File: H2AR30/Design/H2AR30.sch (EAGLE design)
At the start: 57 parts, among them P1 HEXABIT__NO_P1_P5_P6_P7_P12, U2 INA199B2DCKT, U3 INA199B1DCKT, U4 TEXAS_INSTRUMENTS_REF2033AIDD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, X1 XTALL_CSTCE8M00G52

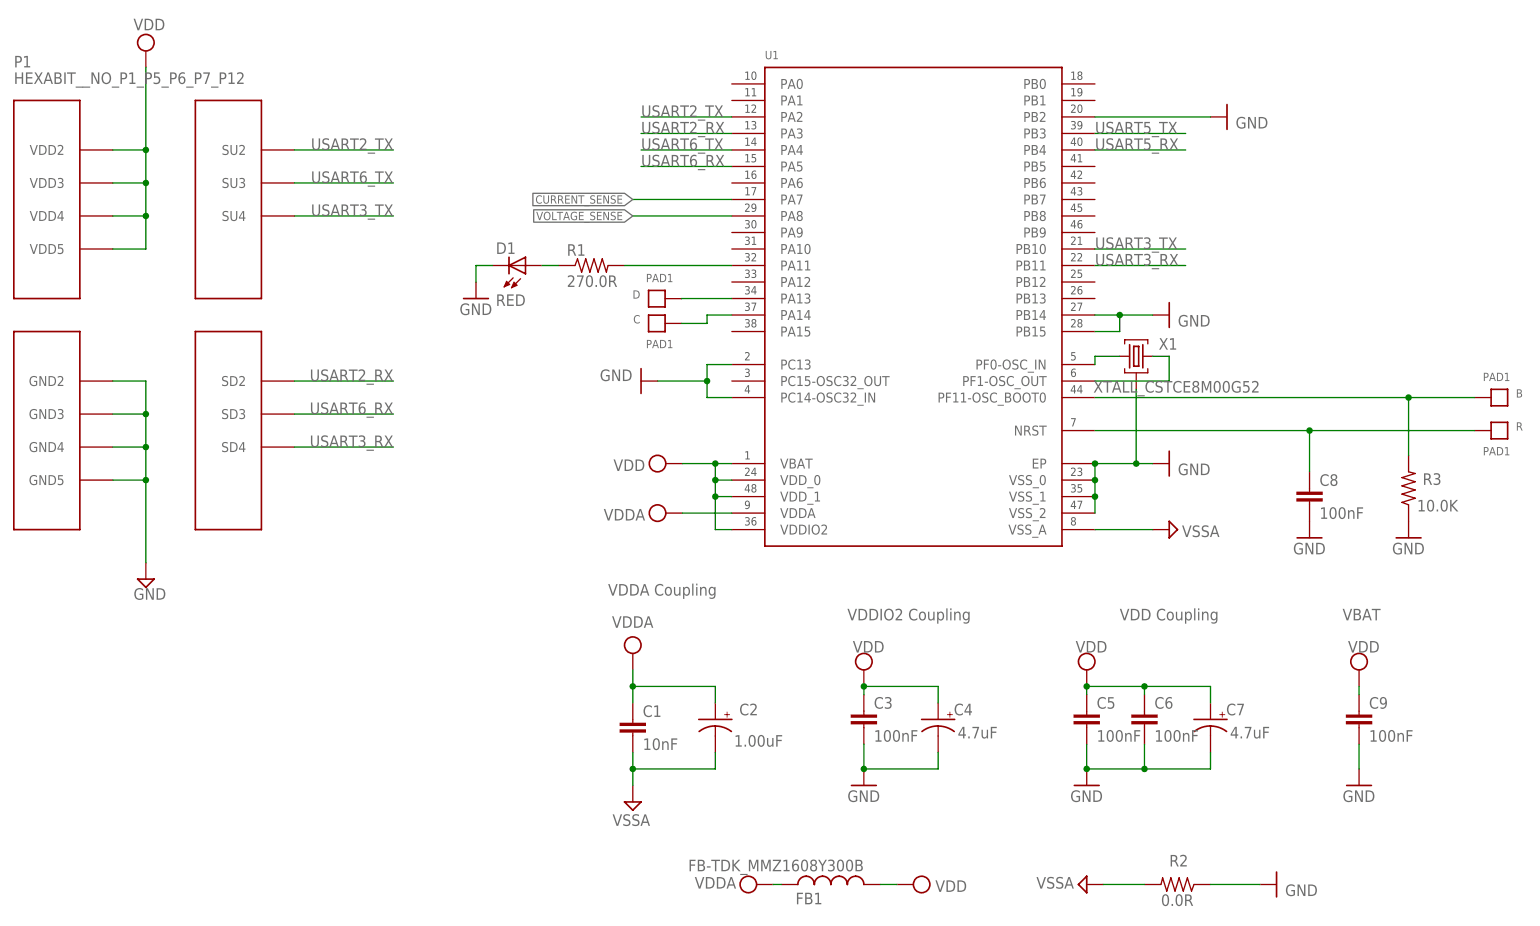
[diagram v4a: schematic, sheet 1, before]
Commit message: Final Design: High voltage logos were added High voltage clearance checked * were added to boot pins 100A & 4A (optional ) CTs  were added to BOM ERC & DRC were made
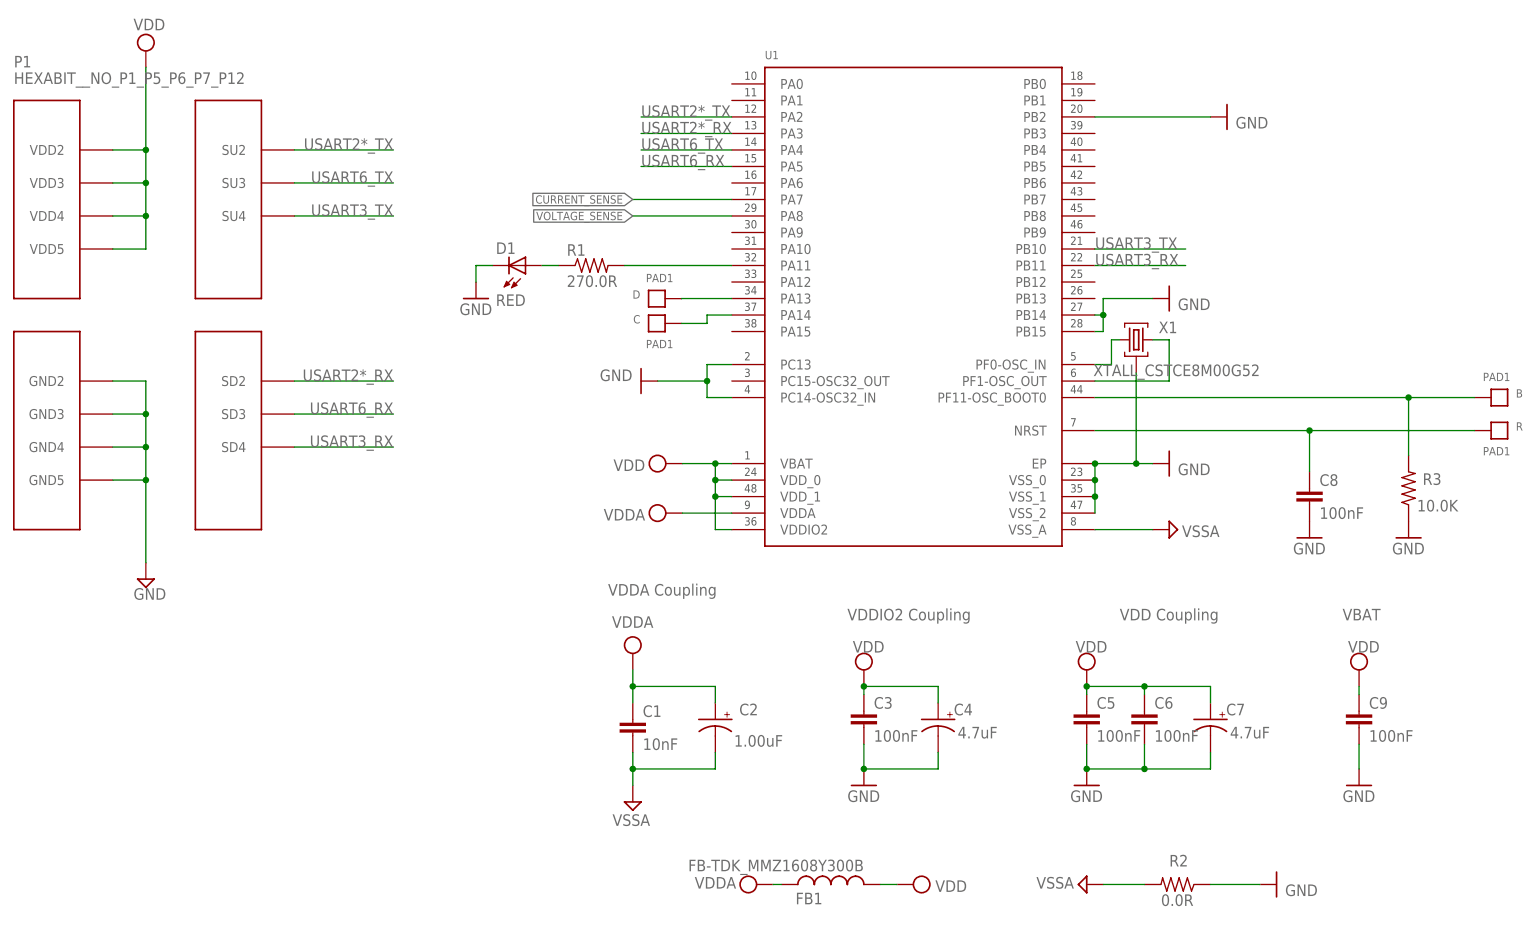
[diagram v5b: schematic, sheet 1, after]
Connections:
- net USART2_RX renamed USART2*_RX
- net USART2_TX renamed USART2*_TX
- removed net USART5_RX: U1.PB4
- removed net USART5_TX: U1.PB3
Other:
- moved on the sheet: X1
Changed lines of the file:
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@@
 <setting verticaltext="up"/>
 </settings>
-<grid distance="0.1" unitdist="inch" unit="inch" style="lines" multiple="1" display="no" altdistance="0.01" altunitdist="inch" altunit="inch"/>
+<grid distance="50" unitdist="mil" unit="mil" style="lines" multiple="1" display="no" altdistance="0.01" altunitdist="inch" altunit="inch"/>
 <layers>
 <layer number="1" name="Top" color="4" fill="1" visible="no" active="no"/>
@@
 <attribute name="OCTOPART_URL" value="https://octopart.com/rt1206brd071ml-yageo-1262221?r=sp"/>
 </part>
-<part name="U3" library="HEXABITZ_ICs" library_urn="urn:adsk.eagle:library:20064554" deviceset="INA199B1DCKT" device="" package3d_urn="urn:adsk.eagle:package:19904117/2" value="INA199B1DCKT"/>
+<part name="U3" library="HEXABITZ_ICs" library_urn="urn:adsk.eagle:library:20064554" deviceset="INA199B1DCKT" device="" package3d_urn="urn:adsk.eagle:package:19904117/4" value="INA199B1DCKT"/>
 <part name="C16" library="HEXABITZ_RCLS" library_urn="urn:adsk.eagle:library:20064561" deviceset="C-0603" device="" package3d_urn="urn:adsk.eagle:package:19666468/2" value="10uF">
 <attribute name="CAPACITANCE" value="10uF"/>
@@
 <part name="GND11" library="supply1" library_urn="urn:adsk.eagle:library:371" deviceset="GND" device=""/>
 <part name="P1" library="hexabitz_connectors" library_urn="urn:adsk.eagle:library:20064578" deviceset="HEXABIT_?_NO_P1_P5_P6_P7_P12" device="" package3d_urn="urn:adsk.eagle:package:20748456/3"/>
-<part name="U2" library="HEXABITZ_ICs" library_urn="urn:adsk.eagle:library:20064554" deviceset="INA199B2DCKT" device="" package3d_urn="urn:adsk.eagle:package:19904117/2"/>
+<part name="U2" library="HEXABITZ_ICs" library_urn="urn:adsk.eagle:library:20064554" deviceset="INA199B2DCKT" device="" package3d_urn="urn:adsk.eagle:package:19904117/4"/>
 </parts>
 <sheets>
@@
 <attribute name="VALUE" x="99.568" y="145.415" size="1.778" layer="96" rot="MR180"/>
 </instance>
-<instance part="X1" gate="G$1" x="198.12" y="135.89" smashed="yes">
-<attribute name="NAME" x="204.47" y="138.684" size="1.778" layer="95" rot="R180"/>
-<attribute name="VALUE" x="217.17" y="132.08" size="1.778" layer="96" rot="R180"/>
+<instance part="X1" gate="G$1" x="198.12" y="138.43" smashed="yes">
+<attribute name="NAME" x="204.47" y="141.224" size="1.778" layer="95" rot="R180"/>
+<attribute name="VALUE" x="217.17" y="134.62" size="1.778" layer="96" rot="R180"/>
 </instance>
 <instance part="GND1" gate="1" x="96.52" y="144.78" smashed="yes">
@@
 <attribute name="VALUE" x="43.815" y="98.425" size="1.778" layer="96"/>
 </instance>
-<instance part="GND9" gate="1" x="203.2" y="142.24" smashed="yes" rot="R90">
-<attribute name="VALUE" x="209.55" y="142.24" size="1.778" layer="96" rot="R180"/>
+<instance part="GND9" gate="1" x="203.2" y="144.78" smashed="yes" rot="R90">
+<attribute name="VALUE" x="209.55" y="144.78" size="1.778" layer="96" rot="R180"/>
 </instance>
 <instance part="GND10" gate="1" x="121.92" y="132.08" smashed="yes" rot="R270">
@@
 <wire x1="191.77" y1="114.3" x2="191.77" y2="116.84" width="0.1524" layer="91"/>
 <wire x1="191.77" y1="116.84" x2="191.77" y2="119.38" width="0.1524" layer="91"/>
-<wire x1="198.12" y1="130.81" x2="198.12" y2="119.38" width="0.1524" layer="91"/>
+<wire x1="198.12" y1="133.35" x2="198.12" y2="119.38" width="0.1524" layer="91"/>
 <junction x="191.77" y="119.38"/>
 <pinref part="U1" gate="G$1" pin="VSS_0"/>
@@
 </segment>
 <segment>
-<pinref part="GND9" gate="1" pin="GND"/>
-<wire x1="200.66" y1="142.24" x2="195.58" y2="142.24" width="0.1524" layer="91"/>
-<pinref part="U1" gate="G$1" pin="PB14"/>
-<pinref part="U1" gate="G$1" pin="PB15"/>
-<wire x1="195.58" y1="142.24" x2="191.77" y2="142.24" width="0.1524" layer="91"/>
-<wire x1="191.77" y1="139.7" x2="195.58" y2="139.7" width="0.1524" layer="91"/>
-<wire x1="195.58" y1="139.7" x2="195.58" y2="142.24" width="0.1524" layer="91"/>
-<junction x="195.58" y="142.24"/>
-</segment>
-<segment>
 <pinref part="U1" gate="G$1" pin="PC14-OSC32_IN"/>
 <wire x1="135.89" y1="129.54" x2="132.08" y2="129.54" width="0.1524" layer="91"/>
@@
 <wire x1="191.77" y1="172.72" x2="209.55" y2="172.72" width="0.1524" layer="91"/>
 </segment>
-</net>
-<net name="USART5_TX" class="0">
-<segment>
-<pinref part="U1" gate="G$1" pin="PB3"/>
-<wire x1="191.77" y1="170.18" x2="205.74" y2="170.18" width="0.1524" layer="91"/>
-<label x="191.77" y="170.18" size="1.778" layer="95"/>
-</segment>
-</net>
-<net name="USART5_RX" class="0">
 <segment>
-<pinref part="U1" gate="G$1" pin="PB4"/>
-<wire x1="191.77" y1="167.64" x2="205.74" y2="167.64" width="0.1524" layer="91"/>
-<label x="191.77" y="167.64" size="1.778" layer="95"/>
+<pinref part="U1" gate="G$1" pin="PB14"/>
+<pinref part="U1" gate="G$1" pin="PB15"/>
+<wire x1="193.04" y1="142.24" x2="191.77" y2="142.24" width="0.1524" layer="91"/>
+<wire x1="191.77" y1="139.7" x2="193.04" y2="139.7" width="0.1524" layer="91"/>
+<wire x1="193.04" y1="139.7" x2="193.04" y2="142.24" width="0.1524" layer="91"/>
+<wire x1="193.04" y1="142.24" x2="193.04" y2="144.78" width="0.1524" layer="91"/>
+<junction x="193.04" y="142.24"/>
+<pinref part="GND9" gate="1" pin="GND"/>
+<wire x1="193.04" y1="144.78" x2="200.66" y2="144.78" width="0.1524" layer="91"/>
 </segment>
 </net>
@@
 <net name="N$5" class="0">
 <segment>
-<pinref part="U1" gate="G$1" pin="PF0-OSC_IN"/>
-<wire x1="191.77" y1="134.62" x2="191.77" y2="135.89" width="0.1524" layer="91"/>
 <pinref part="X1" gate="G$1" pin="1"/>
-<wire x1="191.77" y1="135.89" x2="195.58" y2="135.89" width="0.1524" layer="91"/>
+<wire x1="194.31" y1="138.43" x2="195.58" y2="138.43" width="0.1524" layer="91"/>
+<pinref part="U1" gate="G$1" pin="PF0-OSC_IN"/>
+<wire x1="191.77" y1="134.62" x2="194.31" y2="134.62" width="0.1524" layer="91"/>
+<wire x1="194.31" y1="134.62" x2="194.31" y2="138.43" width="0.1524" layer="91"/>
 </segment>
 </net>
@@
 <pinref part="U1" gate="G$1" pin="PF1-OSC_OUT"/>
 <wire x1="191.77" y1="132.08" x2="203.2" y2="132.08" width="0.1524" layer="91"/>
-<wire x1="203.2" y1="132.08" x2="203.2" y2="135.89" width="0.1524" layer="91"/>
+<wire x1="203.2" y1="132.08" x2="203.2" y2="138.43" width="0.1524" layer="91"/>
 <pinref part="X1" gate="G$1" pin="3"/>
-<wire x1="203.2" y1="135.89" x2="200.66" y2="135.89" width="0.1524" layer="91"/>
+<wire x1="203.2" y1="138.43" x2="200.66" y2="138.43" width="0.1524" layer="91"/>
 </segment>
 </net>
@@
 </segment>
 </net>
-<net name="USART2_TX" class="0">
+<net name="USART2*_TX" class="0">
 <segment>
 <pinref part="U1" gate="G$1" pin="PA2"/>
@@
 </segment>
 </net>
-<net name="USART2_RX" class="0">
+<net name="USART2*_RX" class="0">
 <segment>
 <pinref part="U1" gate="G$1" pin="PA3"/>
@@
 <wire x1="40.64" y1="181.61" x2="30.48" y2="181.61" width="0.1524" layer="91"/>
 <wire x1="40.64" y1="177.8" x2="40.64" y2="181.61" width="0.1524" layer="91"/>
+<junction x="40.64" y="181.61"/>
 </segment>
 <segment>

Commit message: final with double check
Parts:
- added R16: 1M0, HEXABITZ_RCLS:R_1206R1206
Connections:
- removed net N$24: R10.2, R9.1
- removed net N$25: R8.1, R9.2
- new net N$10: R16.1, R9.2
- new net N$13: R10.2, R8.1
- new net N$22: D3.1, FB5.1, R14.1, R9.1
- net GND: now also U1.PB0
- net NEUTRAL: now also R16.2; no longer D3.1, FB5.1, R14.1
- net VCC: no longer U4.VREF
- net VOLTAGE_SENSE: now also U1.PB1; no longer U1.PA8
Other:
- moved on the sheet: R8, R9
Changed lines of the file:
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@@
 <?xml version="1.0" encoding="utf-8"?>
 <!DOCTYPE eagle SYSTEM "eagle.dtd">
-<eagle version="9.6.1">
+<eagle version="9.6.2">
 <drawing>
 <settings>
@@
 <setting verticaltext="up"/>
 </settings>
-<grid distance="50" unitdist="mil" unit="mil" style="lines" multiple="1" display="no" altdistance="0.01" altunitdist="inch" altunit="inch"/>
+<grid distance="0.05" unitdist="inch" unit="inch" style="lines" multiple="1" display="no" altdistance="0.01" altunitdist="inch" altunit="inch"/>
 <layers>
 <layer number="1" name="Top" color="4" fill="1" visible="no" active="no"/>
@@
 <part name="SUPPLY26" library="supply2" deviceset="VCC" device="" value="VDDA"/>
 <part name="SUPPLY28" library="supply2" deviceset="VCC" device="" value="VDDA"/>
-<part name="SUPPLY32" library="supply2" deviceset="VCC" device="" value="VDDA"/>
 <part name="SUPPLY15" library="supply2" deviceset="AGND" device="" value="VSSA"/>
 <part name="SUPPLY25" library="supply2" deviceset="AGND" device="" value="VSSA"/>
@@
 <part name="P1" library="hexabitz_connectors" library_urn="urn:adsk.eagle:library:20064578" deviceset="HEXABIT_?_NO_P1_P5_P6_P7_P12" device="" package3d_urn="urn:adsk.eagle:package:20748456/3"/>
 <part name="U2" library="HEXABITZ_ICs" library_urn="urn:adsk.eagle:library:20064554" deviceset="INA199B2DCKT" device="" package3d_urn="urn:adsk.eagle:package:19904117/4"/>
+<part name="R16" library="HEXABITZ_RCLS" library_urn="urn:adsk.eagle:library:20064561" deviceset="R_1206" device="R1206" package3d_urn="urn:adsk.eagle:package:20937486/1" value="1M0">
+<spice>
+<pinmapping spiceprefix="R">
+<pinmap gate="G$1" pin="1" pinorder="1"/>
+<pinmap gate="G$1" pin="2" pinorder="2"/>
+</pinmapping>
+</spice>
+<attribute name="MFN" value="Yageo"/>
+<attribute name="MPN" value="RT1206BRD071ML"/>
+<attribute name="OCTOPART_URL" value="https://octopart.com/rt1206brd071ml-yageo-1262221?r=sp"/>
+</part>
+<part name="GND12" library="supply1" library_urn="urn:adsk.eagle:library:371" deviceset="GND" device=""/>
 </parts>
 <sheets>
@@
 <attribute name="VALUE" x="25.4" y="177.8" size="1.778" layer="96"/>
 </instance>
+<instance part="GND12" gate="1" x="212.09" y="177.8" smashed="yes" rot="R90">
+<attribute name="VALUE" x="218.44" y="177.8" size="1.778" layer="96" rot="R180"/>
+</instance>
 </instances>
 <busses>
@@
 <wire x1="193.04" y1="144.78" x2="200.66" y2="144.78" width="0.1524" layer="91"/>
 </segment>
+<segment>
+<pinref part="U1" gate="G$1" pin="PB0"/>
+<pinref part="GND12" gate="1" pin="GND"/>
+<wire x1="191.77" y1="177.8" x2="209.55" y2="177.8" width="0.1524" layer="91"/>
+</segment>
 </net>
 <net name="USART3_TX" class="0">
@@
 <net name="VOLTAGE_SENSE" class="0">
 <segment>
-<pinref part="U1" gate="G$1" pin="PA8"/>
-<wire x1="135.89" y1="157.48" x2="120.65" y2="157.48" width="0.1524" layer="91"/>
-<label x="120.65" y="157.48" size="1.27" layer="95" rot="R180" xref="yes"/>
+<pinref part="U1" gate="G$1" pin="PB1"/>
+<wire x1="191.77" y1="175.26" x2="223.52" y2="175.26" width="0.1524" layer="91"/>
+<label x="223.52" y="175.26" size="1.27" layer="95" xref="yes"/>
 </segment>
 </net>
@@
 <attribute name="VALUE" x="110.617" y="159.385" size="1.778" layer="96" rot="R180"/>
 </instance>
-<instance part="R8" gate="G$1" x="41.91" y="129.54" smashed="yes" rot="R90">
-<attribute name="NAME" x="44.45" y="132.3086" size="1.778" layer="95"/>
-<attribute name="VALUE" x="44.45" y="126.238" size="1.778" layer="96"/>
-</instance>
-<instance part="R9" gate="G$1" x="41.91" y="116.84" smashed="yes" rot="R90">
+<instance part="R8" gate="G$1" x="41.91" y="116.84" smashed="yes" rot="R90">
 <attribute name="NAME" x="44.45" y="119.6086" size="1.778" layer="95"/>
 <attribute name="VALUE" x="44.45" y="113.538" size="1.778" layer="96"/>
 </instance>
+<instance part="R9" gate="G$1" x="34.29" y="86.36" smashed="yes" rot="R180">
+<attribute name="NAME" x="31.5214" y="88.9" size="1.778" layer="95" rot="R90"/>
+<attribute name="VALUE" x="37.592" y="88.9" size="1.778" layer="96" rot="R90"/>
+</instance>
 <instance part="R10" gate="G$1" x="41.91" y="104.14" smashed="yes" rot="R90">
 <attribute name="NAME" x="44.45" y="106.9086" size="1.778" layer="95"/>
@@
 <attribute name="VALUE" x="173.355" y="73.025" size="1.778" layer="96" rot="R180"/>
 </instance>
-<instance part="SUPPLY32" gate="G$1" x="208.28" y="52.07" smashed="yes" rot="R270">
-<attribute name="VALUE" x="213.995" y="48.895" size="1.778" layer="96" rot="R90"/>
-</instance>
 <instance part="SUPPLY15" gate="G$1" x="125.73" y="34.29" smashed="yes">
 <attribute name="VALUE" x="128.397" y="32.385" size="1.778" layer="96" rot="R180"/>
@@
 <attribute name="VALUE" x="171.2976" y="143.0782" size="2.0828" layer="96" ratio="10" rot="SR0"/>
 </instance>
+<instance part="R16" gate="G$1" x="22.86" y="86.36" smashed="yes" rot="R180">
+<attribute name="NAME" x="20.0914" y="88.9" size="1.778" layer="95" rot="R90"/>
+<attribute name="VALUE" x="26.162" y="88.9" size="1.778" layer="96" rot="R90"/>
+</instance>
 </instances>
 <busses>
@@
 </segment>
 <segment>
-<pinref part="U4" gate="G$0" pin="VREF"/>
-<wire x1="205.74" y1="52.07" x2="205.74" y2="52.324" width="0.1524" layer="91"/>
-<wire x1="205.74" y1="52.324" x2="204.47" y2="52.324" width="0.1524" layer="91"/>
-<pinref part="SUPPLY32" gate="G$1" pin="VCC"/>
-</segment>
-<segment>
 <pinref part="SUPPLY14" gate="G$1" pin="VCC"/>
 <pinref part="C14" gate="G$1" pin="1"/>
@@
 </segment>
 </net>
-<net name="NEUTRAL" class="0">
+<net name="N$22" class="0">
 <segment>
 <pinref part="D3" gate="G$0" pin="1"/>
@@
 <wire x1="64.77" y1="86.36" x2="41.91" y2="86.36" width="0.1524" layer="91"/>
 <junction x="64.77" y="86.36"/>
-<wire x1="41.91" y1="86.36" x2="41.91" y2="81.28" width="0.1524" layer="91"/>
-<wire x1="41.91" y1="81.28" x2="30.48" y2="81.28" width="0.1524" layer="91"/>
 <pinref part="R14" gate="G$1" pin="1"/>
 <wire x1="41.91" y1="86.36" x2="41.91" y2="87.63" width="0.1524" layer="91"/>
 <junction x="41.91" y="86.36"/>
-<label x="30.48" y="81.28" size="1.778" layer="95"/>
-</segment>
-<segment>
-<wire x1="44.45" y1="31.75" x2="57.15" y2="31.75" width="0.1524" layer="91"/>
-<label x="46.99" y="31.75" size="1.778" layer="95"/>
-<pinref part="P2" gate="G$1" pin="1"/>
-</segment>
-</net>
-<net name="N$24" class="0">
-<segment>
-<pinref part="R10" gate="G$1" pin="2"/>
+<wire x1="41.91" y1="86.36" x2="39.37" y2="86.36" width="0.1524" layer="91"/>
 <pinref part="R9" gate="G$1" pin="1"/>
-<wire x1="41.91" y1="109.22" x2="41.91" y2="111.76" width="0.1524" layer="91"/>
-</segment>
-</net>
-<net name="N$25" class="0">
-<segment>
-<pinref part="R9" gate="G$1" pin="2"/>
-<pinref part="R8" gate="G$1" pin="1"/>
-<wire x1="41.91" y1="121.92" x2="41.91" y2="124.46" width="0.1524" layer="91"/>
 </segment>
 </net>
@@
 <segment>
 <pinref part="R8" gate="G$1" pin="2"/>
-<wire x1="41.91" y1="134.62" x2="41.91" y2="137.16" width="0.1524" layer="91"/>
-<wire x1="41.91" y1="137.16" x2="30.48" y2="137.16" width="0.1524" layer="91"/>
-<label x="30.48" y="137.16" size="1.778" layer="95"/>
+<wire x1="41.91" y1="121.92" x2="41.91" y2="124.46" width="0.1524" layer="91"/>
+<wire x1="41.91" y1="124.46" x2="30.48" y2="124.46" width="0.1524" layer="91"/>
+<label x="30.48" y="124.46" size="1.778" layer="95"/>
 </segment>
 <segment>
@@
 </segment>
 </net>
+<net name="N$10" class="0">
+<segment>
+<pinref part="R9" gate="G$1" pin="2"/>
+<wire x1="29.21" y1="86.36" x2="27.94" y2="86.36" width="0.1524" layer="91"/>
+<pinref part="R16" gate="G$1" pin="1"/>
+</segment>
+</net>
+<net name="N$13" class="0">
+<segment>
+<pinref part="R10" gate="G$1" pin="2"/>
+<pinref part="R8" gate="G$1" pin="1"/>
+<wire x1="41.91" y1="111.76" x2="41.91" y2="109.22" width="0.1524" layer="91"/>
+</segment>
+</net>
+<net name="NEUTRAL" class="0">
+<segment>
+<pinref part="R16" gate="G$1" pin="2"/>
+<wire x1="17.78" y1="86.36" x2="7.62" y2="86.36" width="0.1524" layer="91"/>
+<label x="7.62" y="86.36" size="1.778" layer="95"/>
+</segment>
+<segment>
+<pinref part="P2" gate="G$1" pin="1"/>
+<wire x1="44.45" y1="31.75" x2="57.15" y2="31.75" width="0.1524" layer="91"/>
+<label x="46.99" y="31.75" size="1.778" layer="95"/>
+</segment>
+</net>
